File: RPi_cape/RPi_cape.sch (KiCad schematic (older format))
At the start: 108 parts, among them J1 Conn_01x04, J10 Conn_01x02, J11 Conn_01x02, J12 Conn_01x02, J16 Conn_01x06, J2 Conn_01x02, J3 Conn_01x02, J4 Conn_01x02, J5 Conn_01x03, J6 Conn_01x03, J7 Conn_01x02, J8 Conn_02x20_Odd_Even, J9 Conn_01x02, U1 TL431A, U2 ADC128D818, U3 ADC128D818

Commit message: Docs cleanup
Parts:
- C3: Part Number GCM32EC71H106KA03 -> GCM32EC71H106KA03L
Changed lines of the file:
@@
 F 3 "~" H 3600 2800 50  0001 C CNN
 F 4 "Murata" H 3600 2800 50  0001 C CNN "Manufacturer"
-F 5 "GCM32EC71H106KA03" H 3600 2800 50  0001 C CNN "Part Number"
+F 5 "GCM32EC71H106KA03L" H 3600 2800 50  0001 C CNN "Part Number"
 	1    3600 2800
 	-1   0    0    -1

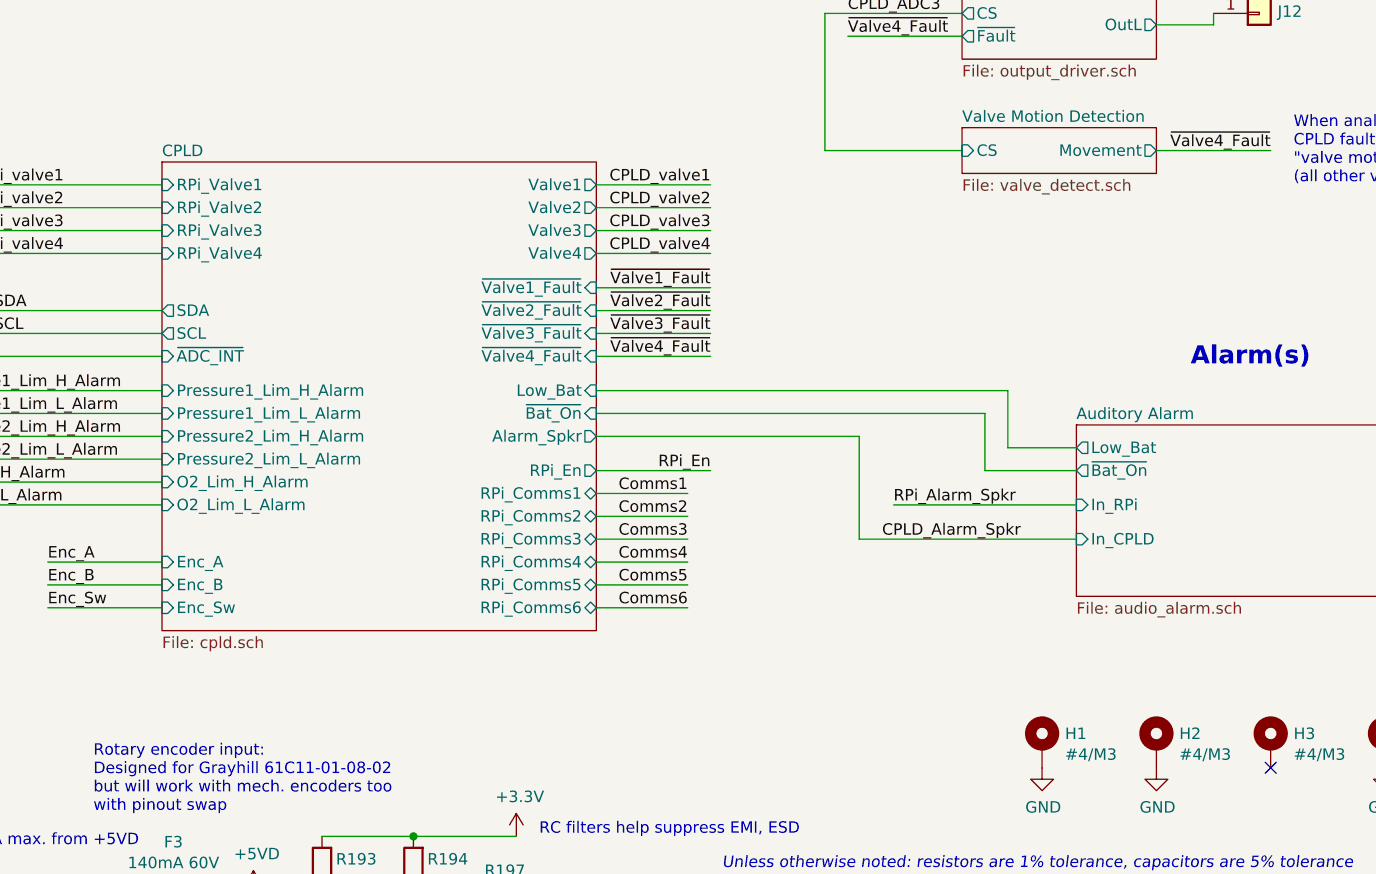
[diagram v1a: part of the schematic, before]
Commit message: +5VA outage detection
Separated +1.8V and +5VA monitoring and added +3.3V output for +5VA on ~5VA_On signal to CPLD, to cover an extra failure mode
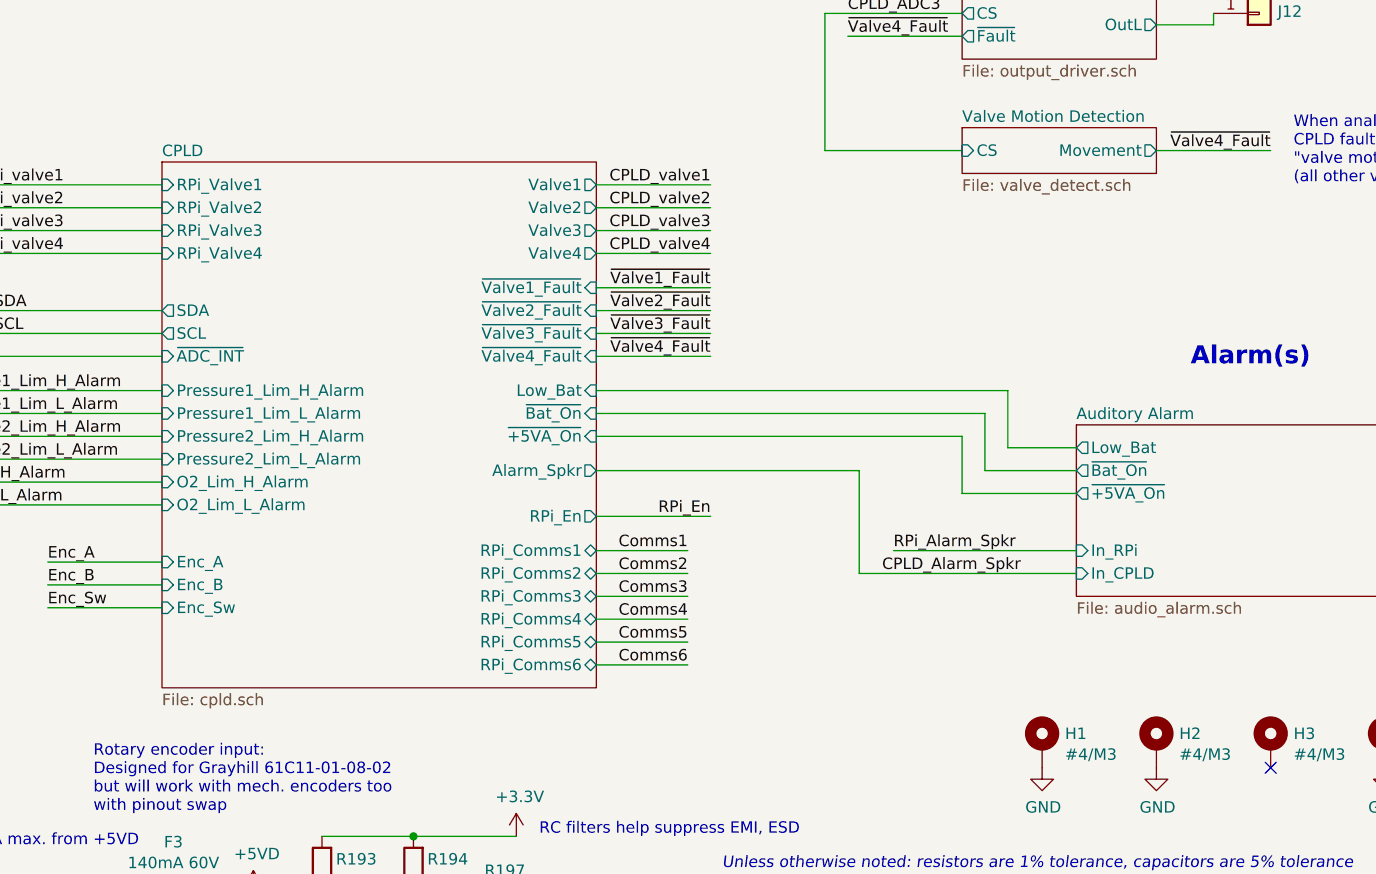
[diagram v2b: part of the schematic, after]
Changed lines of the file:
@@
 Title "Raspberry Pi Hat for JamVent Adaptation"
 Date ""
-Rev "1.6"
+Rev "1.7"
 Comp "Partners COVID Innovation Group"
 Comment1 "Don Straney"
@@
 F0 "Auditory Alarm" 50
 F1 "audio_alarm.sch" 50
-F2 "In_RPi" I L 13850 7750 50
-F3 "In_CPLD" I L 13850 7900 50
+F2 "In_RPi" I L 13850 7950 50
+F3 "In_CPLD" I L 13850 8050 50
 F4 "Low_Bat" O L 13850 7500 50
 F5 "~Bat_On" O L 13850 7600 50
+F6 "~+5VA_On" O L 13850 7700 50
 $EndSheet
 $Comp
@@
 GPIO9
 Wire Wire Line
-	12900 7450 12900 7900
+	12900 7600 12900 8050
 Wire Wire Line
-	12900 7900 13850 7900
-Text Label 13000 7900 0    50   ~ 0
+	12900 8050 13850 8050
+Text Label 13000 8050 0    50   ~ 0
 CPLD_Alarm_Spkr
 Wire Wire Line
-	13050 7750 13850 7750
-Text Label 13050 7750 0    50   ~ 0
+	13050 7950 13850 7950
+Text Label 13050 7950 0    50   ~ 0
 RPi_Alarm_Spkr
 $Sheet
@@
 	11750 7250 13550 7250
 Wire Wire Line
-	11750 7450 12900 7450
+	11750 7600 12900 7600
 Wire Wire Line
-	11750 7700 12150 7700
+	11750 7950 12150 7950
 Wire Wire Line
-	11750 7800 12150 7800
+	11750 8050 12150 8050
 Wire Wire Line
-	11750 7900 12150 7900
+	11750 8150 12150 8150
 Wire Wire Line
-	11750 8000 12150 8000
+	11750 8250 12150 8250
 Wire Wire Line
-	11750 8100 12150 8100
+	11750 8350 12150 8350
 Wire Wire Line
-	11750 8200 12150 8200
-Text Label 12150 7700 2    50   ~ 0
+	11750 8450 12150 8450
+Text Label 12150 7950 2    50   ~ 0
 Comms1
-Text Label 12150 7800 2    50   ~ 0
+Text Label 12150 8050 2    50   ~ 0
 Comms2
-Text Label 12150 7900 2    50   ~ 0
+Text Label 12150 8150 2    50   ~ 0
 Comms3
-Text Label 12150 8000 2    50   ~ 0
+Text Label 12150 8250 2    50   ~ 0
 Comms4
-Text Label 12150 8100 2    50   ~ 0
+Text Label 12150 8350 2    50   ~ 0
 Comms5
-Text Label 12150 8200 2    50   ~ 0
+Text Label 12150 8450 2    50   ~ 0
 Comms6
 Text Notes 11650 2750 0    50   ~ 0
@@
 $EndComp
 Wire Wire Line
-	11750 7600 12250 7600
-Text Label 12250 7600 2    50   ~ 0
+	11750 7800 12250 7800
+Text Label 12250 7800 2    50   ~ 0
 RPi_En
 Text Notes 12300 9350 0    50   Italic 0
@@
 	13450 7350 11750 7350
 $Sheet
-S 9850 6250 1900 2050
+S 9850 6250 1900 2300
 U 5E8C8865
 F0 "CPLD" 50
@@
 F14 "O2_Lim_H_Alarm" I L 9850 7650 50
 F15 "O2_Lim_L_Alarm" I L 9850 7750 50
-F16 "Alarm_Spkr" O R 11750 7450 50
+F16 "Alarm_Spkr" O R 11750 7600 50
 F17 "SDA" O L 9850 6900 50
 F18 "SCL" O L 9850 7000 50
 F19 "~ADC_INT" I L 9850 7100 50
 F20 "Low_Bat" I R 11750 7250 50
-F21 "RPi_Comms1" B R 11750 7700 50
-F22 "RPi_Comms2" B R 11750 7800 50
-F23 "RPi_Comms3" B R 11750 7900 50
-F24 "RPi_Comms4" B R 11750 8000 50
-F25 "RPi_Comms5" B R 11750 8100 50
-F26 "RPi_Comms6" B R 11750 8200 50
-F27 "RPi_En" O R 11750 7600 50
+F21 "RPi_Comms1" B R 11750 7950 50
+F22 "RPi_Comms2" B R 11750 8050 50
+F23 "RPi_Comms3" B R 11750 8150 50
+F24 "RPi_Comms4" B R 11750 8250 50
+F25 "RPi_Comms5" B R 11750 8350 50
+F26 "RPi_Comms6" B R 11750 8450 50
+F27 "RPi_En" O R 11750 7800 50
 F28 "Enc_A" I L 9850 8000 50
 F29 "Enc_B" I L 9850 8100 50
@@
 F34 "~Valve3_Fault" I R 11750 7000 50
 F35 "~Bat_On" I R 11750 7350 50
+F36 "~+5VA_On" I R 11750 7450 50
 $EndSheet
 $Comp
@@
 Text Notes 3050 1700 2    50   ~ 0
 TVS clamps @ 39V max @ 15A,\nvs. cap ratings of 50V, LMZ14203\nabs-max rating of 43V
+Wire Wire Line
+	11750 7450 13350 7450
+Wire Wire Line
+	13350 7450 13350 7700
+Wire Wire Line
+	13350 7700 13850 7700
 $EndSCHEMATC
